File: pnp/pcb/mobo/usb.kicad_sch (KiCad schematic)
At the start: 15 parts, among them J10 AUX USB, J11 Top Camera, J8 Host, J9 Bottom Camera, U10 FE1.1, Y2 12MHz

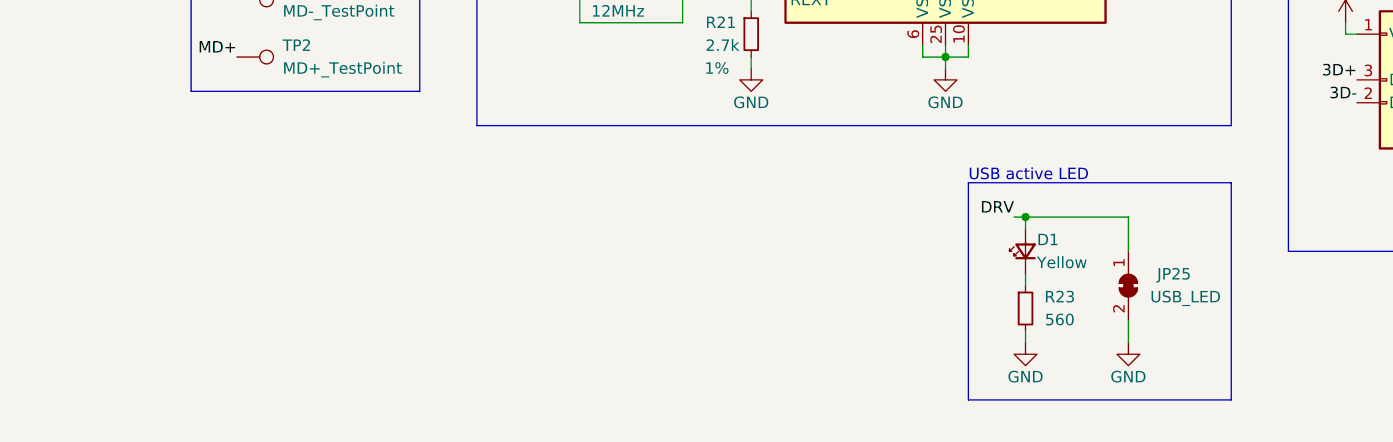
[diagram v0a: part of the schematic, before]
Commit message: first commit of rev04 mobo beta 0. makes solder-selectable jumpers on back side of board not jumped to work with kit drivers, y2 motor port rotated correctly, moves traces out from underneath solder jumpers, adds 0 ohm jumpers to bypass the usb hub, adds 4 pin DIN connector for power, adds large decoupling cap on power supply input to decrease rippling, changes diode choice for 5v multiplexer to one already in the BOM, flips resistors on mos1 to be less confusing
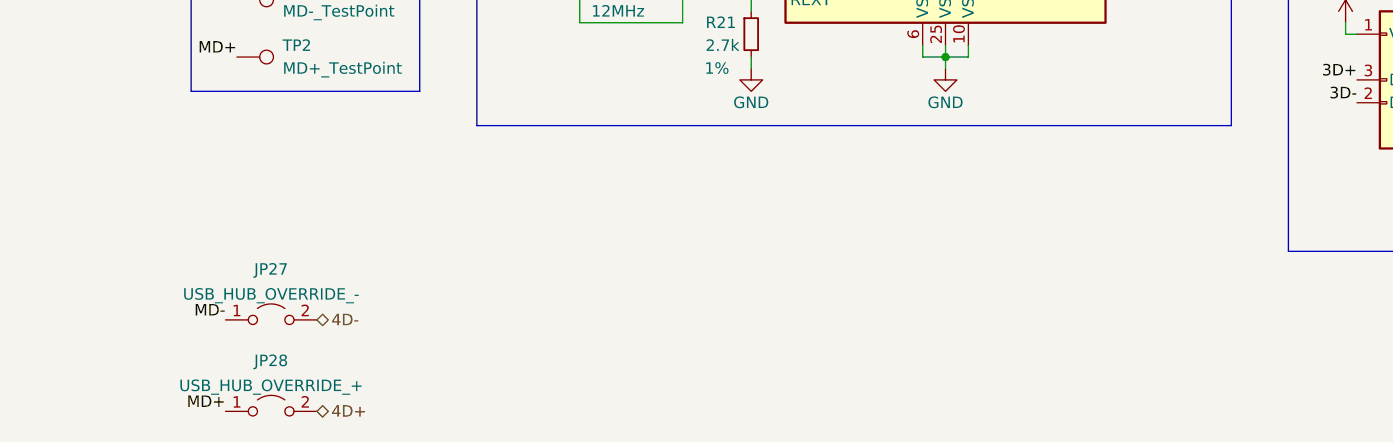
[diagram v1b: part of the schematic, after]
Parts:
- removed D1: Yellow, LED_SMD:LED_0805_2012Metric, symbol Device:LED_Small
- removed JP25: USB_LED, Jumper:SolderJumper-2_P1.3mm_Bridged_RoundedPad1.0x1.5mm, symbol Jumper:SolderJumper_2_Bridged
- removed R23: 560, Resistor_SMD:R_0805_2012Metric, symbol Device:R_Small
- added JP27: USB_HUB_OVERRIDE_-, Resistor_SMD:R_0805_2012Metric_Pad1.20x1.40mm_HandSolder, symbol Jumper:Jumper_2_Open
- added JP28: USB_HUB_OVERRIDE_+, Resistor_SMD:R_0805_2012Metric_Pad1.20x1.40mm_HandSolder, symbol Jumper:Jumper_2_Open
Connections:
- net 4D+: now also JP28.2 (B)
- net 4D-: now also JP27.2 (B)
- net MD+: now also JP28.1 (A)
- net MD-: now also JP27.1 (A)
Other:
- note removed: "USB active LED"
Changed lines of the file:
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@@
   (junction (at 219.71 77.47) (diameter 0) (color 0 0 0 0)
-  )
-  (junction (at 175.26 142.24) (diameter 0) (color 0 0 0 0)
   )
   (junction (at 219.71 107.95) (diameter 0) (color 0 0 0 0)
@@
     (stroke (width 0) (type default) (color 0 0 0 0))
   )
-  (wire (pts (xy 175.26 142.24) (xy 175.26 143.51))
-    (stroke (width 0) (type default) (color 0 0 0 0))
-  )
   (wire (pts (xy 63.5 99.06) (xy 63.5 100.33))
     (stroke (width 0) (type default) (color 0 0 0 0))
@@
     (stroke (width 0) (type default) (color 0 0 0 0))
   )
-  (polyline (pts (xy 168.91 138.43) (xy 168.91 162.56))
-    (stroke (width 0) (type default) (color 0 0 0 0))
-  )
   (wire (pts (xy 146.05 67.31) (xy 144.78 67.31))
     (stroke (width 0) (type default) (color 0 0 0 0))
@@
     (stroke (width 0) (type default) (color 0 0 0 0))
   )
-  (polyline (pts (xy 168.91 138.43) (xy 198.12 138.43))
-    (stroke (width 0) (type default) (color 0 0 0 0))
-  )
   (wire (pts (xy 80.01 76.2) (xy 81.28 76.2))
     (stroke (width 0) (type default) (color 0 0 0 0))
@@
     (stroke (width 0) (type default) (color 0 0 0 0))
   )
-  (wire (pts (xy 186.69 142.24) (xy 186.69 146.05))
-    (stroke (width 0) (type default) (color 0 0 0 0))
-  )
   (wire (pts (xy 91.44 68.58) (xy 78.74 68.58))
     (stroke (width 0) (type default) (color 0 0 0 0))
   )
-  (wire (pts (xy 175.26 148.59) (xy 175.26 149.86))
-    (stroke (width 0) (type default) (color 0 0 0 0))
-  )
-  (polyline (pts (xy 198.12 162.56) (xy 168.91 162.56))
-    (stroke (width 0) (type default) (color 0 0 0 0))
-  )
   (wire (pts (xy 146.05 90.17) (xy 144.78 90.17))
     (stroke (width 0) (type default) (color 0 0 0 0))
@@
     (stroke (width 0) (type default) (color 0 0 0 0))
   )
-  (wire (pts (xy 175.26 154.94) (xy 175.26 156.21))
-    (stroke (width 0) (type default) (color 0 0 0 0))
-  )
   (wire (pts (xy 210.82 59.69) (xy 210.82 60.96))
     (stroke (width 0) (type default) (color 0 0 0 0))
@@
     (stroke (width 0) (type default) (color 0 0 0 0))
   )
-  (wire (pts (xy 175.26 142.24) (xy 173.99 142.24))
-    (stroke (width 0) (type default) (color 0 0 0 0))
-  )
   (wire (pts (xy 176.53 60.96) (xy 176.53 62.23))
     (stroke (width 0) (type default) (color 0 0 0 0))
@@
     (stroke (width 0) (type default) (color 0 0 0 0))
   )
-  (polyline (pts (xy 198.12 138.43) (xy 198.12 162.56))
-    (stroke (width 0) (type default) (color 0 0 0 0))
-  )
   (wire (pts (xy 88.9 59.69) (xy 88.9 60.96))
     (stroke (width 0) (type default) (color 0 0 0 0))
@@
     (stroke (width 0) (type default) (color 0 0 0 0))
   )
-  (wire (pts (xy 186.69 153.67) (xy 186.69 156.21))
-    (stroke (width 0) (type default) (color 0 0 0 0))
-  )
-  (wire (pts (xy 175.26 142.24) (xy 186.69 142.24))
-    (stroke (width 0) (type default) (color 0 0 0 0))
-  )
   (wire (pts (xy 166.37 123.19) (xy 166.37 124.46))
     (stroke (width 0) (type default) (color 0 0 0 0))
@@
     (effects (font (size 1.27 1.27)) (justify left bottom))
   )
-  (text "USB active LED" (at 168.91 138.43 0)
-    (effects (font (size 1.27 1.27)) (justify left bottom))
-  )
   (text "Connection to PC" (at 50.8 52.07 0)
     (effects (font (size 1.27 1.27)) (justify left bottom))
+  )
+  (label "MD-" (at 86.36 153.67 180)
+    (effects (font (size 1.27 1.27)) (justify right bottom))
   )
   (label "MD-" (at 146.05 72.39 180)
@@
     (effects (font (size 1.27 1.27)) (justify left bottom))
   )
-  (label "DRV" (at 173.99 142.24 180)
-    (effects (font (size 1.27 1.27)) (justify right bottom))
-  )
   (label "MD+" (at 81.28 78.74 0)
     (effects (font (size 1.27 1.27)) (justify left bottom))
@@
     (effects (font (size 1.27 1.27)) (justify right bottom))
   )
+  (label "MD+" (at 86.36 163.83 180)
+    (effects (font (size 1.27 1.27)) (justify right bottom))
+  )
+  (hierarchical_label "4D-" (shape bidirectional) (at 96.52 153.67 0)
+    (effects (font (size 1.27 1.27)) (justify left))
+  )
   (hierarchical_label "4D-" (shape bidirectional) (at 186.69 92.71 0)
     (effects (font (size 1.27 1.27)) (justify left))
   )
   (hierarchical_label "4D+" (shape bidirectional) (at 186.69 90.17 0)
+    (effects (font (size 1.27 1.27)) (justify left))
+  )
+  (hierarchical_label "4D+" (shape bidirectional) (at 96.52 163.83 0)
     (effects (font (size 1.27 1.27)) (justify left))
   )
@@
     (pin "1")
   )
-  (symbol (lib_id "Device:LED_Small") (at 175.26 146.05 90) (unit 1)
-    (in_bom yes) (on_board yes)
-    (property "Reference" "D1" (id 0) (at 176.53 144.78 90)
-      (effects (font (size 1.27 1.27)) (justify right))
-    )
-    (property "Value" "Yellow" (id 1) (at 176.53 147.32 90)
-      (effects (font (size 1.27 1.27)) (justify right))
-    )
-    (property "Footprint" "LED_SMD:LED_0805_2012Metric" (id 2) (at 175.26 146.05 0)
-      (effects (font (size 1.27 1.27)) hide)
-    )
-    (property "Datasheet" "" (id 3) (at 175.26 146.05 0)
-      (effects (font (size 1.27 1.27)) hide)
-    )
-    (property "Digikey" "732-4987-1-ND" (id 4) (at 175.26 146.05 0)
-      (effects (font (size 1.27 1.27)) hide)
-    )
-    (property "JLCPCB" "C2296" (id 5) (at 175.26 146.05 0)
-      (effects (font (size 1.27 1.27)) hide)
-    )
-    (property "LCSC" "C779458" (id 6) (at 175.26 146.05 0)
-      (effects (font (size 1.27 1.27)) hide)
-    )
-    (property "Mouser" "710-150080YS75000" (id 7) (at 175.26 146.05 0)
-      (effects (font (size 1.27 1.27)) hide)
-    )
-    (property "Config" "+USBPWR" (id 8) (at 175.26 146.05 0)
-      (effects (font (size 1.27 1.27)) hide)
-    )
-    (pin "1")
-    (pin "2")
-  )
   (symbol (lib_id "power:GND") (at 144.78 102.87 270) (unit 1)
     (in_bom yes) (on_board yes)
@@
     )
     (pin "1")
-  )
-  (symbol (lib_id "Jumper:SolderJumper_2_Bridged") (at 186.69 149.86 270) (unit 1)
-    (in_bom yes) (on_board yes)
-    (property "Reference" "JP25" (id 0) (at 191.77 148.59 90))
-    (property "Value" "USB_LED" (id 1) (at 193.04 151.13 90))
-    (property "Footprint" "Jumper:SolderJumper-2_P1.3mm_Bridged_RoundedPad1.0x1.5mm" (id 2) (at 186.69 149.86 0)
-      (effects (font (size 1.27 1.27)) hide)
-    )
-    (property "Datasheet" "~" (id 3) (at 186.69 149.86 0)
-      (effects (font (size 1.27 1.27)) hide)
-    )
-    (pin "1")
-    (pin "2")
-  )
-  (symbol (lib_id "power:GND") (at 175.26 156.21 0) (unit 1)
-    (in_bom yes) (on_board yes)
-    (property "Reference" "#PWR0132" (id 0) (at 175.26 162.56 0)
-      (effects (font (size 1.27 1.27)) hide)
-    )
-    (property "Value" "GND" (id 1) (at 175.26 160.02 0))
-    (property "Footprint" "" (id 2) (at 175.26 156.21 0)
-      (effects (font (size 1.27 1.27)) hide)
-    )
-    (property "Datasheet" "" (id 3) (at 175.26 156.21 0)
-      (effects (font (size 1.27 1.27)) hide)
-    )
-    (pin "1")
-  )
-  (symbol (lib_id "power:GND") (at 186.69 156.21 0) (unit 1)
-    (in_bom yes) (on_board yes)
-    (property "Reference" "#PWR0135" (id 0) (at 186.69 162.56 0)
-      (effects (font (size 1.27 1.27)) hide)
-    )
-    (property "Value" "GND" (id 1) (at 186.69 160.02 0))
-    (property "Footprint" "" (id 2) (at 186.69 156.21 0)
-      (effects (font (size 1.27 1.27)) hide)
-    )
-    (property "Datasheet" "" (id 3) (at 186.69 156.21 0)
-      (effects (font (size 1.27 1.27)) hide)
-    )
-    (pin "1")
-  )
-  (symbol (lib_id "Device:R_Small") (at 175.26 152.4 0) (unit 1)
-    (in_bom yes) (on_board yes)
-    (property "Reference" "R23" (id 0) (at 179.07 151.13 0))
-    (property "Value" "560" (id 1) (at 179.07 153.67 0))
-    (property "Footprint" "Resistor_SMD:R_0805_2012Metric" (id 2) (at 175.26 152.4 0)
-      (effects (font (size 1.27 1.27)) hide)
-    )
-    (property "Datasheet" "" (id 3) (at 175.26 152.4 0)
-      (effects (font (size 1.27 1.27)) hide)
-    )
-    (property "JLCPCB" "C28636" (id 4) (at 175.26 152.4 0)
-      (effects (font (size 1.27 1.27)) hide)
-    )
-    (property "LCSC" "C28636" (id 5) (at 175.26 152.4 0)
-      (effects (font (size 1.27 1.27)) hide)
-    )
-    (property "Digikey" "RHM560AHCT-ND" (id 6) (at 175.26 152.4 0)
-      (effects (font (size 1.27 1.27)) hide)
-    )
-    (property "Mouser" "667-ERJ-6ENF5600V" (id 7) (at 175.26 152.4 0)
-      (effects (font (size 1.27 1.27)) hide)
-    )
-    (property "Config" "+USBPWR" (id 8) (at 175.26 152.4 0)
-      (effects (font (size 1.27 1.27)) hide)
-    )
-    (pin "1")
-    (pin "2")
   )
   (symbol (lib_id "power:+3.3V") (at 143.51 80.01 90) (unit 1)
@@
     (pin "1")
   )
+  (symbol (lib_id "Jumper:Jumper_2_Open") (at 91.44 163.83 0) (unit 1)
+    (in_bom yes) (on_board yes) (fields_autoplaced)
+    (property "Reference" "JP28" (id 0) (at 91.44 158.2125 0))
+    (property "Value" "USB_HUB_OVERRIDE_+" (id 1) (at 91.44 160.9876 0))
+    (property "Footprint" "Resistor_SMD:R_0805_2012Metric_Pad1.20x1.40mm_HandSolder" (id 2) (at 91.44 163.83 0)
+      (effects (font (size 1.27 1.27)) hide)
+    )
+    (property "Datasheet" "~" (id 3) (at 91.44 163.83 0)
+      (effects (font (size 1.27 1.27)) hide)
+    )
+    (pin "1")
+    (pin "2")
+  )
+  (symbol (lib_id "Jumper:Jumper_2_Open") (at 91.44 153.67 0) (unit 1)
+    (in_bom yes) (on_board yes) (fields_autoplaced)
+    (property "Reference" "JP27" (id 0) (at 91.44 148.0525 0))
+    (property "Value" "USB_HUB_OVERRIDE_-" (id 1) (at 91.44 150.8276 0))
+    (property "Footprint" "Resistor_SMD:R_0805_2012Metric_Pad1.20x1.40mm_HandSolder" (id 2) (at 91.44 153.67 0)
+      (effects (font (size 1.27 1.27)) hide)
+    )
+    (property "Datasheet" "~" (id 3) (at 91.44 153.67 0)
+      (effects (font (size 1.27 1.27)) hide)
+    )
+    (pin "1")
+    (pin "2")
+  )
 )

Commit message: another huge chunk of work on rev04 of the mobo. breaks out diag and index pin for TMC2209 sensorless homing. reduces unique part count by consolidating resistor values where possible. replaces full ADC pipeline with monolithic I2C vacuum sensor and an I2C multiplexer due to address collision issues with two sensors. adds solder selectable jumpers for selecting whether an axis uses switch or TMC homing. redoes lots of routing of the SPI lines up to the stepper drivers.
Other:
- company: (none) -> Opulo
- title: Index Mobo -> LumenPnP Motherboard
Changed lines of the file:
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@@
   (paper "A4")
   (title_block
-    (title "Index Mobo")
+    (title "LumenPnP Motherboard")
     (date "2022-03-29")
     (rev "003")
+    (company "Opulo")
   )
   (junction (at 144.78 92.71) (diameter 0) (color 0 0 0 0)
